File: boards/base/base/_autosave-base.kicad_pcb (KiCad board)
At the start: 2 copper layers, 70.9 x 71 mm, 26 parts, among them J1 Conn_01x04_Female, J2 Conn_01x06_Female, J3 Conn_01x06_Female, J4 Screw_Terminal_01x02, J5 Conn_01x03_Female, J6 Conn_01x02_Male, Q1 BC547, Q2 BC547, Q3 2SD1047, Q4 BCP56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

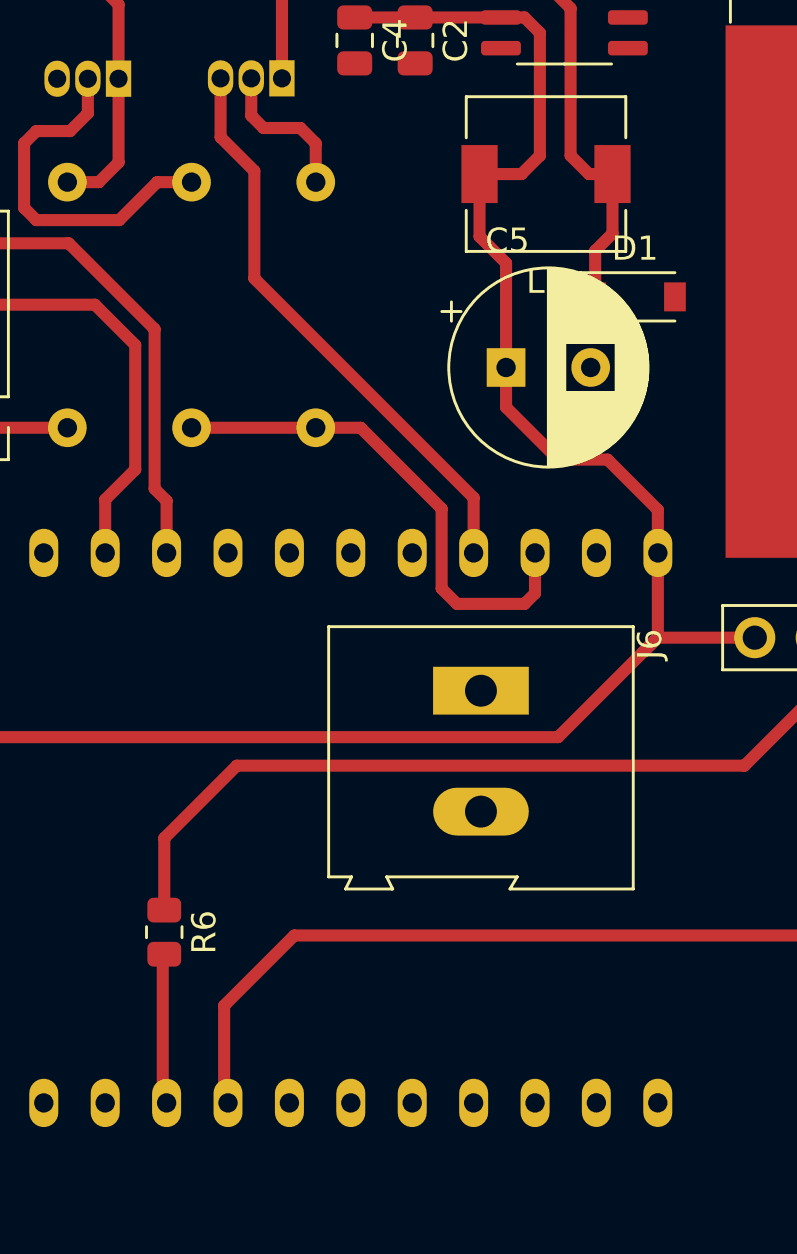
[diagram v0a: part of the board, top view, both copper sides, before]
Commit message: Added cab_reset and base LED
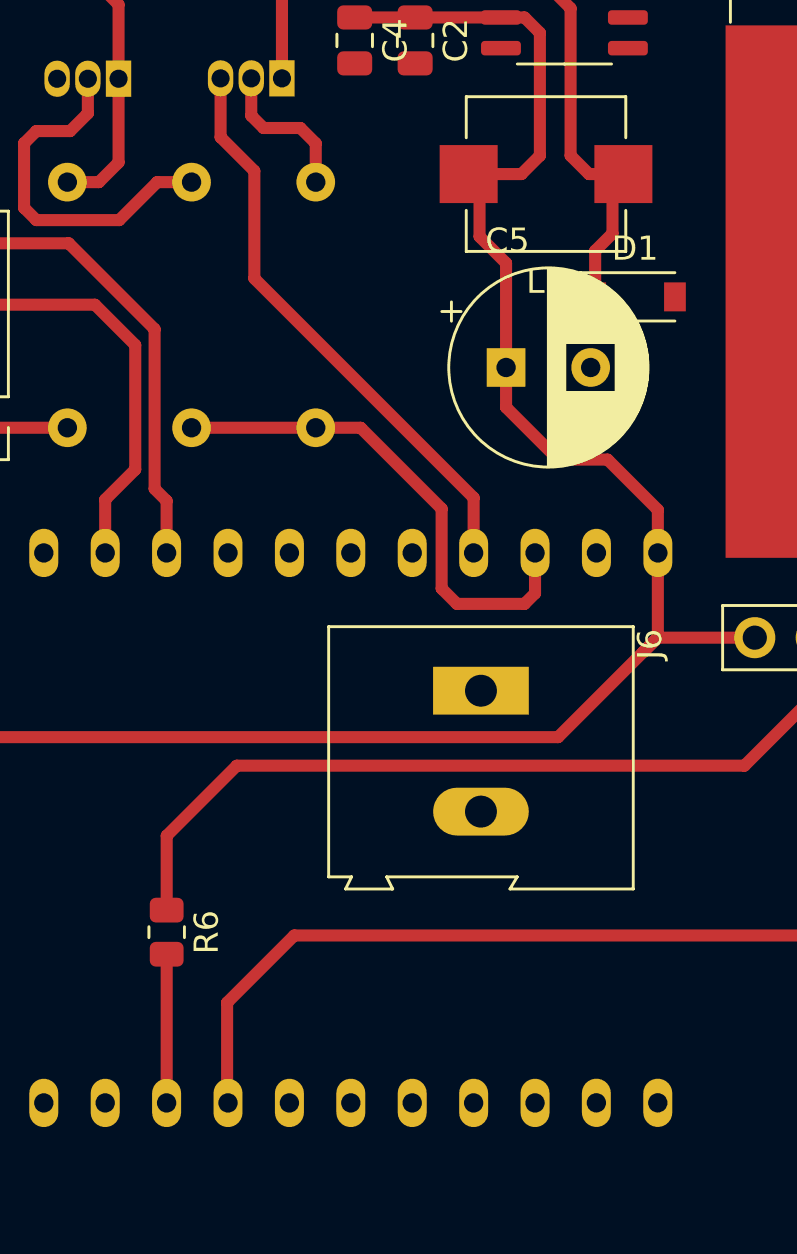
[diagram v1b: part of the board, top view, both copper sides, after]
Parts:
- moved R6 0.10 mm to (102.8, 103.0)
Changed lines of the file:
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@@
   )
   (footprint "Resistor_SMD:R_0805_2012Metric" (layer "F.Cu")
-    (at 102.7 102.9875 -90)
+    (at 102.8 102.9875 -90)
     (descr "Resistor SMD 0805 (2012 Metric), square (rectangular) end terminal, IPC_7351 nominal, (Body size source: IPC-SM-782 page 72, https://www.pcb-3d.com/wordpress/wp-content/uploads/ipc-sm-782a_amendment_1_and_2.pdf), generated with kicad-footprint-generator")
     (tags "resistor")
@@
     (fp_arc (start -1.91 -1.91) (mid 0 -2.701148) (end 1.91 -1.91) (layer "F.Fab") (width 0.1))
     (fp_arc (start 1.91 1.91) (mid 0 2.701148) (end -1.91 1.91) (layer "F.Fab") (width 0.1))
-    (pad "1" smd rect (at -2.75 0 180) (size 1.5 2.4) (layers "F.Cu" "F.Paste" "F.Mask")
+    (pad "1" smd rect (at -3.2 0 180) (size 2.4 2.4) (layers "F.Cu" "F.Paste" "F.Mask")
       (net 4 "Net-(D1-Pad1)") (pinfunction "1") (pintype "passive"))
-    (pad "2" smd rect (at 2.75 0 180) (size 1.5 2.4) (layers "F.Cu" "F.Paste" "F.Mask")
+    (pad "2" smd rect (at 3.2 0 180) (size 2.4 2.4) (layers "F.Cu" "F.Paste" "F.Mask")
       (net 3 "5V") (pinfunction "2") (pintype "passive"))
     (model "${KICAD6_3DMODEL_DIR}/Inductor_SMD.3dshapes/L_6.3x6.3_H3.wrl"
@@
   (segment (start 88.646 58.674) (end 89.916 57.404) (width 0.5) (layer "F.Cu") (net 38))
   (segment (start 91.24 49.73) (end 101.28 49.73) (width 0.5) (layer "F.Cu") (net 38))
-  (segment (start 105.17656 106.02444) (end 105.17656 109.652) (width 0.5) (layer "F.Cu") (net 50))
+  (segment (start 138.176 96.52) (end 131.572 103.124) (width 0.5) (layer "F.Cu") (net 50))
   (segment (start 131.572 103.124) (end 108.077 103.124) (width 0.5) (layer "F.Cu") (net 50))
   (segment (start 138.176 80.518) (end 138.176 96.52) (width 0.5) (layer "F.Cu") (net 50))
-  (segment (start 108.077 103.124) (end 105.17656 106.02444) (width 0.5) (layer "F.Cu") (net 50))
-  (segment (start 138.176 96.52) (end 131.572 103.124) (width 0.5) (layer "F.Cu") (net 50))
+  (segment (start 105.3 105.901) (end 105.3 109.77544) (width 0.5) (layer "F.Cu") (net 50))
+  (segment (start 108.077 103.124) (end 105.3 105.901) (width 0.5) (layer "F.Cu") (net 50))
   (segment (start 85.598 76.708) (end 85.598 80.2405) (width 0.5) (layer "F.Cu") (net 51))
-  (segment (start 102.7 103.9) (end 102.63656 103.96344) (width 0.5) (layer "F.Cu") (net 52))
-  (segment (start 102.63656 103.96344) (end 102.63656 109.652) (width 0.5) (layer "F.Cu") (net 52))
+  (segment (start 102.8 110.04656) (end 102.79656 110.05) (width 0.5) (layer "F.Cu") (net 52))
+  (segment (start 102.8 103.9) (end 102.8 110.04656) (width 0.5) (layer "F.Cu") (net 52))
   (segment (start 129.667 93.133) (end 126.7 96.1) (width 0.5) (layer "F.Cu") (net 53))
   (segment (start 126.7 96.1) (end 105.7 96.1) (width 0.5) (layer "F.Cu") (net 53))
-  (segment (start 105.7 96.1) (end 102.7 99.1) (width 0.5) (layer "F.Cu") (net 53))
+  (segment (start 102.8 99) (end 102.8 102.075) (width 0.5) (layer "F.Cu") (net 53))
+  (segment (start 105.7 96.1) (end 102.8 99) (width 0.5) (layer "F.Cu") (net 53))
   (segment (start 129.667 90.805) (end 129.667 93.133) (width 0.5) (layer "F.Cu") (net 53))
-  (segment (start 102.7 99.1) (end 102.7 102.075) (width 0.5) (layer "F.Cu") (net 53))
   (zone (net 2) (net_name "GND") (layer "F.Cu") (hatch edge 0.508)
     (connect_pads (clearance 0.508))
